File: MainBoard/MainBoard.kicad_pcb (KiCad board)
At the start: 4 copper layers, 40 x 39.4 mm, 76 parts, among them IC1 MAX30102, IC2 TESEO-LIV3F, J1 USB_C_Receptacle_USB2.0, J2 Micro_SD_Card, J3 Conn_01x30_Female, Q1 DMG2301L, SW1 SW_DIP_x01, SW2 SW_DIP_x01, SW3 SW_DIP_x01, U1 MCP73831-2-OT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

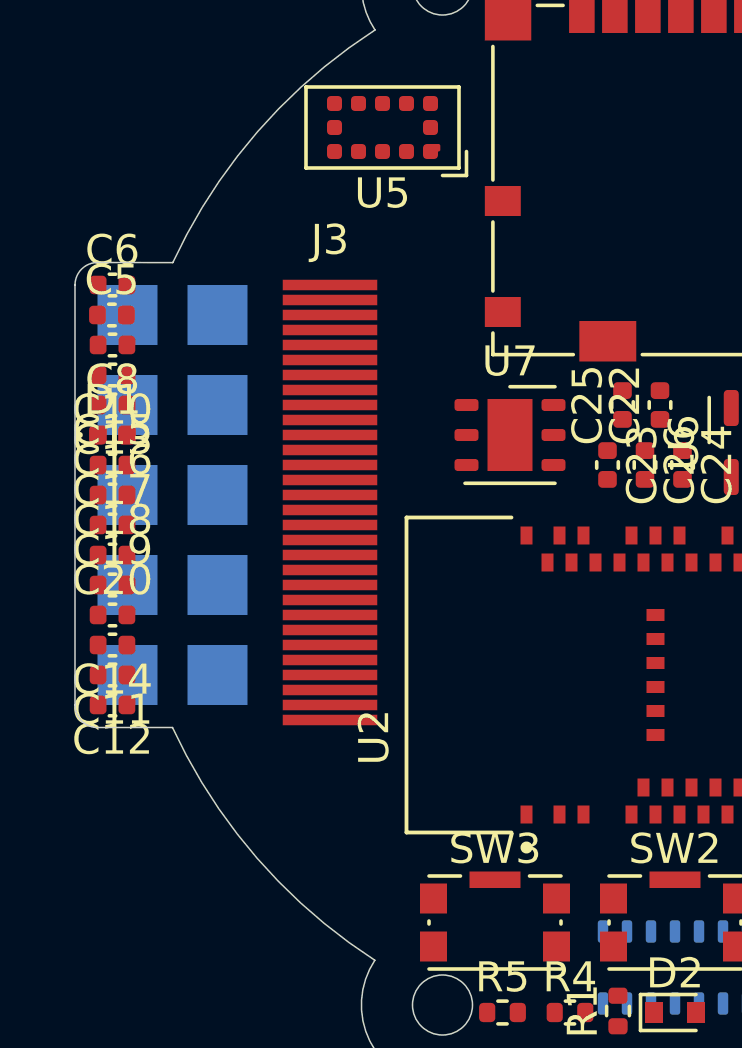
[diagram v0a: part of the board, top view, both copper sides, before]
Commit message: oops! I forgot the buzzer
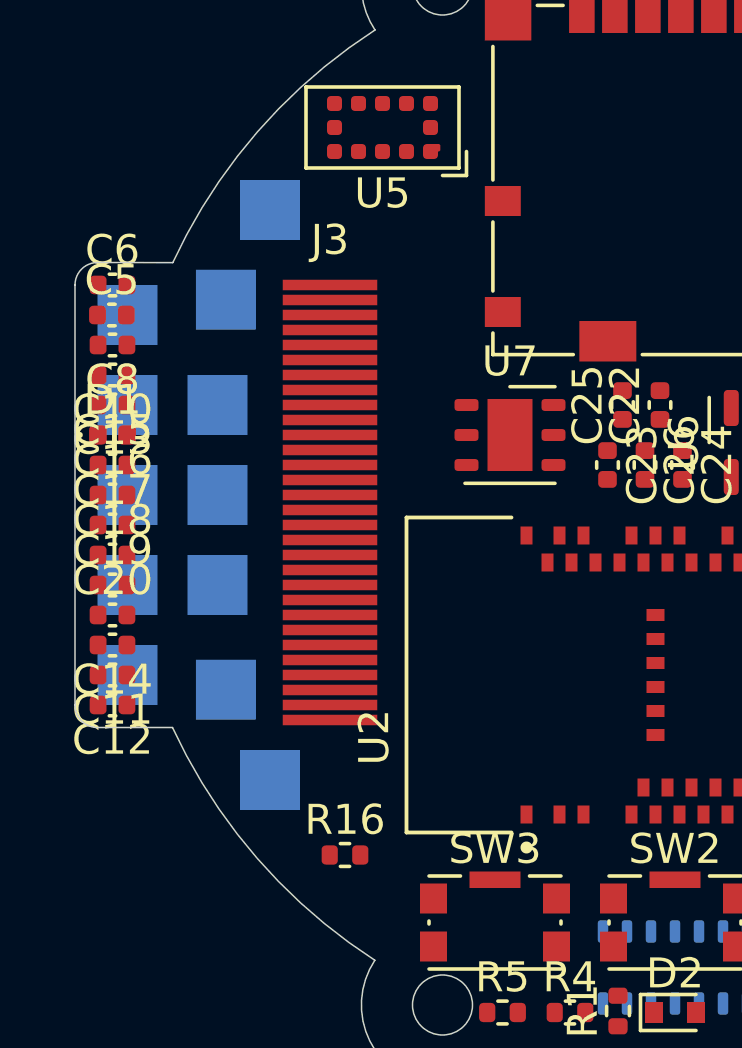
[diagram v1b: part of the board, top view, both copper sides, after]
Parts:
- added BZ1: Buzzer, libs:PB9.11-5v, B.Cu at (118.5, 38.5)
- added R16: 100k, Resistor_SMD:R_0402_1005Metric, F.Cu at (122.5, 50.5)
- moved TP1 3.91 mm to (120.0, 29.0)
- moved TP4 3.91 mm to (120.0, 48.0)

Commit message: route board
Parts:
- added TP9: NFC2, TestPoint:TestPoint_Pad_2.0x2.0mm, B.Cu at (129.5, 21.6)
- R16: value 100k -> JUST IN CASE
- TP8: value NEOPIX -> NFC1
- moved TP8 24.8 mm to (137.5, 21.6)
- moved TP4 13.3 mm to (115.5, 35.5)
- moved TP6 12.6 mm to (119.5, 48.0)
- moved TP10 12.0 mm to (115.5, 32.5)
- moved TP7 7.77 mm to (119.5, 29.0)
- moved TP1 6.67 mm to (118.5, 35.5)
- moved R2 6.10 mm to (140.0, 50.5)
- moved TP14 6.01 mm to (115.5, 44.5)
- moved TP2 4.07 mm to (115.5, 41.5)
- moved TP5 3.01 mm to (115.5, 38.5)
- moved TP3 0.25 mm to (118.5, 41.5)
- turned D1 to 180 degrees
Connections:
- TP8 pad 1: Net-(D5-Pad1) -> Net-(TP8-Pad1)
- U2 pad 52: Net-(U2-Pad52) -> Net-(TP8-Pad1)
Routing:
- net SDA: track 0.00 -> 102.0 mm, vias 0 -> 8
- net GND: track 0.00 -> 92.6 mm, vias 0 -> 26
- net +3V3: track 0.00 -> 74.7 mm, vias 0 -> 17
- net SCL: track 0.00 -> 74.6 mm, vias 0 -> 6
- net Net-(R10-Pad2): track 0.00 -> 59.4 mm, vias 0 -> 4
- net Net-(C2-Pad1): track 0.00 -> 48.3 mm, vias 0 -> 1
- net SPI1-SCK: track 0.00 -> 44.9 mm, vias 0 -> 3
- net Net-(BZ1-Pad1): track 0.00 -> 44.4 mm, vias 0 -> 1
- net Net-(J1-PadA4): track 0.00 -> 39.8 mm, vias 0 -> 1
- net Net-(L1-Pad2): track 0.00 -> 39.7 mm, vias 0 -> 2
- net SPI1-MOSI: track 0.00 -> 38.8 mm, vias 0 -> 3
- net Net-(J3-Pad9): track 0.00 -> 31.3 mm, vias 0 -> 2
- net Net-(BT1-Pad1): track 0.00 -> 31.0 mm, vias 0 -> 2
- net Net-(IC2-Pad9): track 0.00 -> 30.8 mm
- net Net-(J3-Pad8): track 0.00 -> 30.8 mm, vias 0 -> 2
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- added copper zone on B.Cu, net +3V3
- added copper zone on In1.Cu, net +3V3
- added copper zone on F.Cu, net GND
- added copper zone on In2.Cu, net GND
